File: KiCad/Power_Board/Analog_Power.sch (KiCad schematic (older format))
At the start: 73 parts, among them P10 CONN_02X01, P8 CONN_02X01, P9 CONN_02X01, Q1 IRLL024NQ, U10 ADP7142_CSP, U11 ADP7182_CSP, U12 ADP3335_CSP, U7 MAX152x, U8 ADP5070, U9 TPS63030

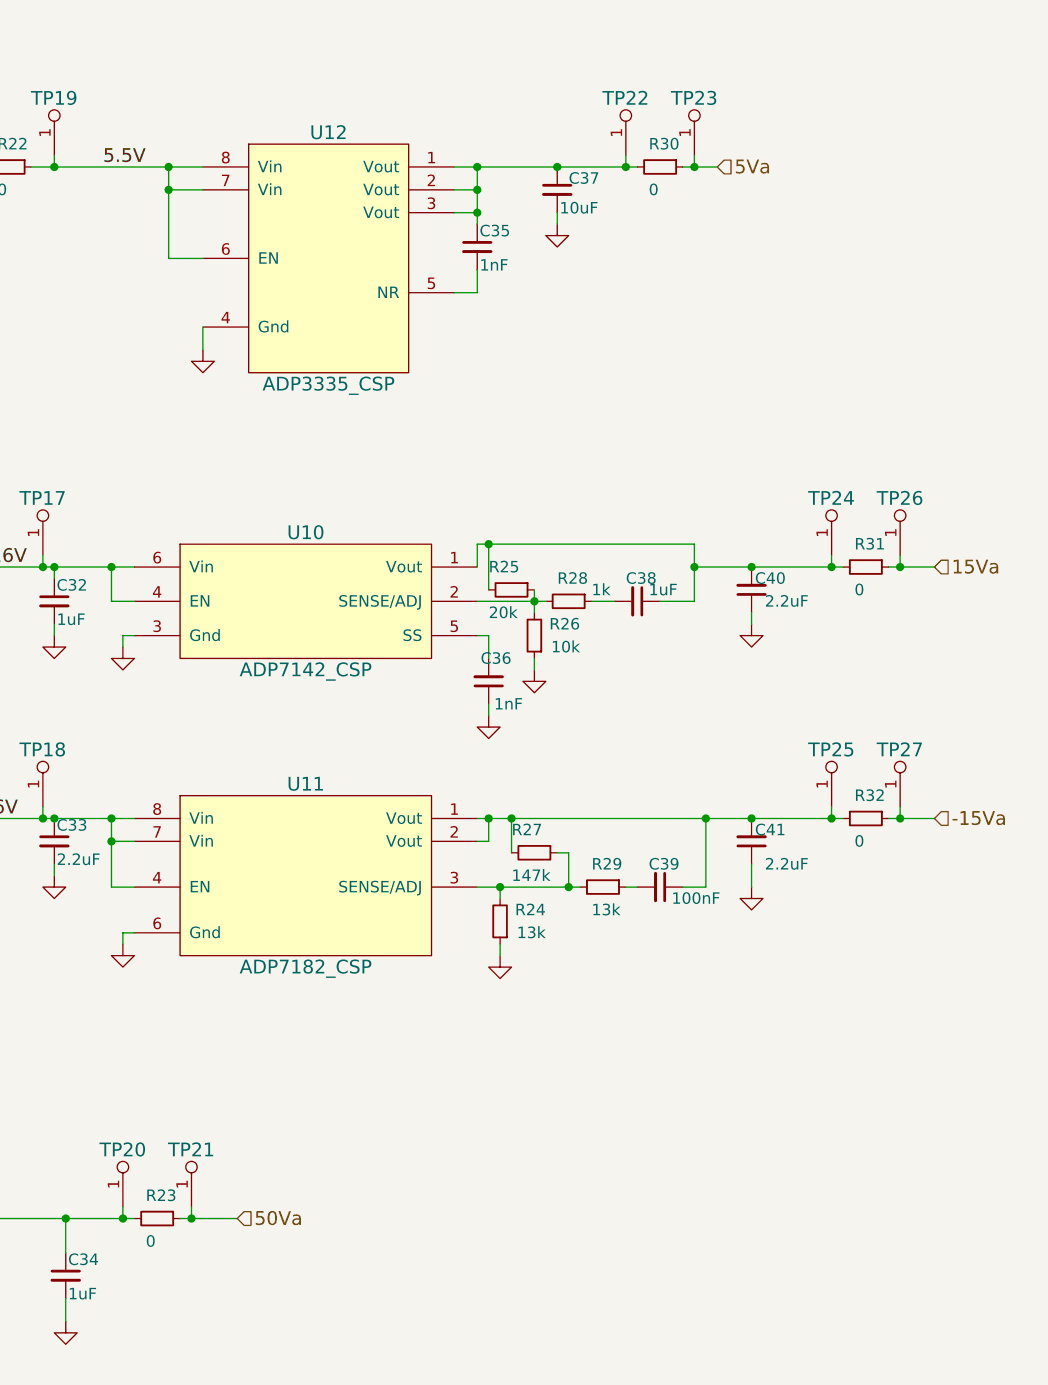
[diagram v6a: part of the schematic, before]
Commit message: Removed redundant SMD test points where test clips are being used.
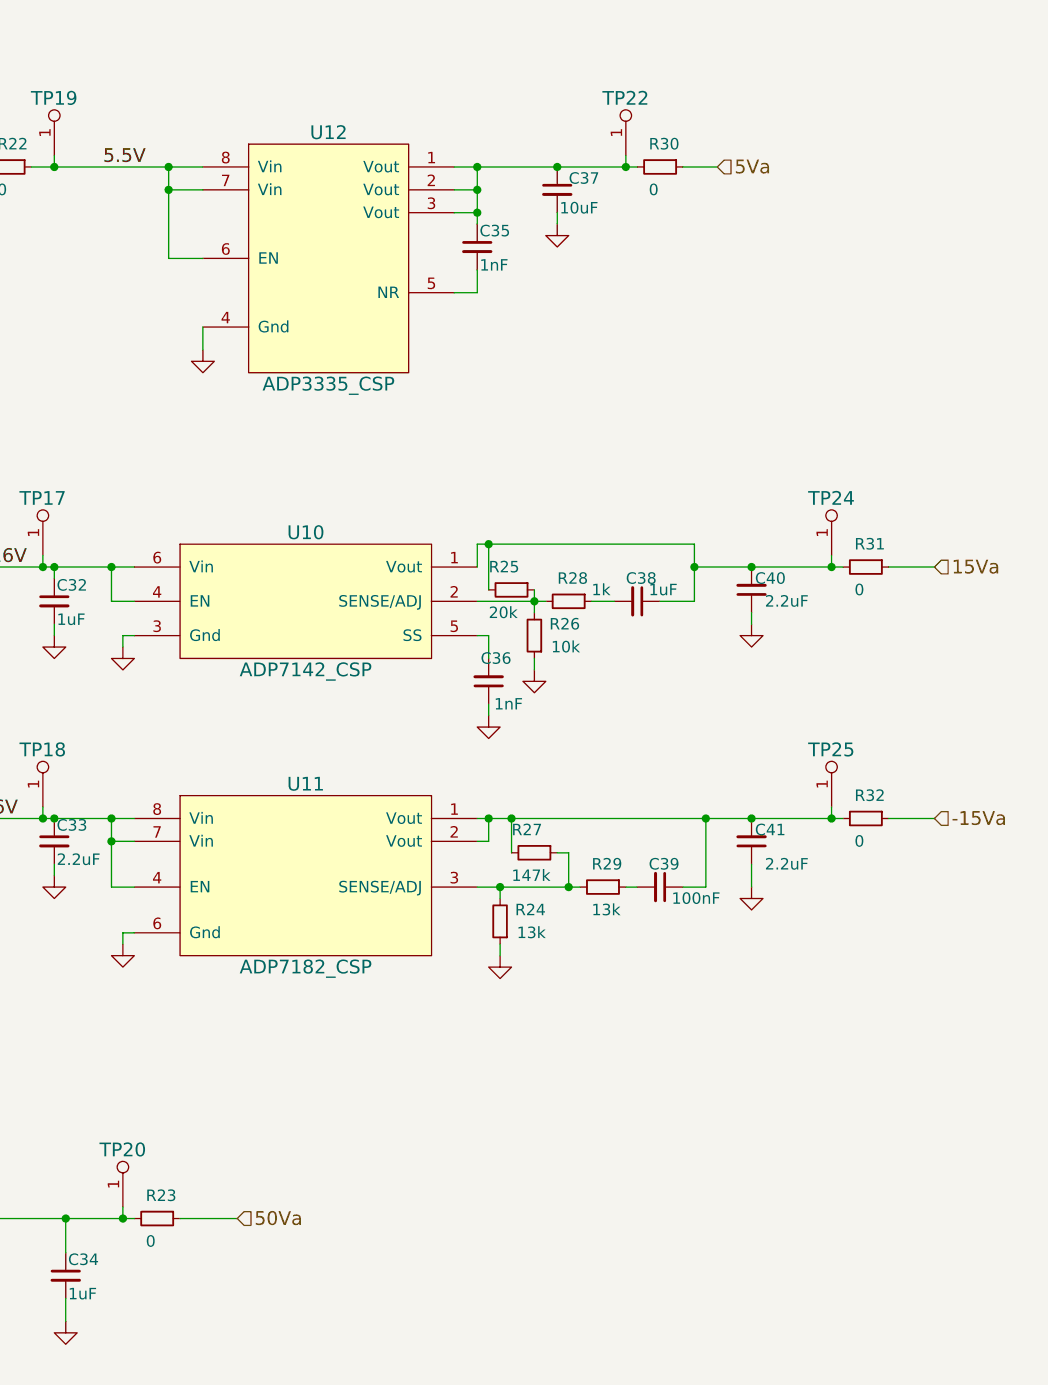
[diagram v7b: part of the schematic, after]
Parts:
- removed TP21, TP23, TP26, TP27: Test_Point, OpenCamera:TEST_POINT_SMD, symbol Test_Point
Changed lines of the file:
@@
 Connection ~ 5900 1400
 $Comp
-L GND #PWR033
+L GND #PWR035
 U 1 1 55902E67
 P 6050 2100
-F 0 "#PWR033" H 6050 1850 50  0001 C CNN
+F 0 "#PWR035" H 6050 1850 50  0001 C CNN
 F 1 "GND" H 6050 1950 50  0001 C CNN
 F 2 "" H 6050 2100 60  0000 C CNN
@@
 Wire Wire Line
 	8150 1300 8300 1300
-$Comp
-L Test_Point TP23
-U 1 1 559056BA
-P 8200 1250
-F 0 "TP23" H 8200 1500 60  0000 C CNN
-F 1 "Test_Point" H 8200 1600 60  0001 C CNN
-F 2 "OpenCamera:TEST_POINT_SMD" H 8200 1250 60  0001 C CNN
-F 3 "" H 8200 1250 60  0000 C CNN
-	1    8200 1250
-	1    0    0    -1
-$EndComp
 Wire Wire Line
 	7900 1250 7900 1300
 Connection ~ 7900 1300
-Wire Wire Line
-	8200 1250 8200 1300
-Connection ~ 8200 1300
-$Comp
-L GND #PWR034
+$Comp
+L GND #PWR036
 U 1 1 55900DFE
 P 4600 1850
-F 0 "#PWR034" H 4600 1600 50  0001 C CNN
+F 0 "#PWR036" H 4600 1600 50  0001 C CNN
 F 1 "GND" H 4600 1700 50  0001 C CNN
 F 2 "" H 4600 1850 60  0000 C CNN
@@
 $EndComp
 $Comp
-L GND #PWR035
+L GND #PWR037
 U 1 1 55900DF8
 P 4000 1850
-F 0 "#PWR035" H 4000 1600 50  0001 C CNN
+F 0 "#PWR037" H 4000 1600 50  0001 C CNN
 F 1 "GND" H 4000 1700 50  0001 C CNN
 F 2 "" H 4000 1850 60  0000 C CNN
@@
 $EndComp
 $Comp
-L GND #PWR036
+L GND #PWR038
 U 1 1 55900DF2
 P 3800 1850
-F 0 "#PWR036" H 3800 1600 50  0001 C CNN
+F 0 "#PWR038" H 3800 1600 50  0001 C CNN
 F 1 "GND" H 3800 1700 50  0001 C CNN
 F 2 "" H 3800 1850 60  0000 C CNN
@@
 $EndComp
 $Comp
-L GND #PWR037
+L GND #PWR039
 U 1 1 55900DDA
 P 2250 1800
-F 0 "#PWR037" H 2250 1550 50  0001 C CNN
+F 0 "#PWR039" H 2250 1550 50  0001 C CNN
 F 1 "GND" H 2250 1650 50  0001 C CNN
 F 2 "" H 2250 1800 60  0000 C CNN
@@
 	1600 2900 1500 2900
 $Comp
-L GND #PWR038
+L GND #PWR040
 U 1 1 5590B69B
 P 1250 2950
-F 0 "#PWR038" H 1250 2700 50  0001 C CNN
+F 0 "#PWR040" H 1250 2700 50  0001 C CNN
 F 1 "GND" H 1250 2800 50  0001 C CNN
 F 2 "" H 1250 2950 60  0000 C CNN
@@
 Connection ~ 1600 3450
 $Comp
-L GND #PWR039
+L GND #PWR041
 U 1 1 5590CBE4
 P 1550 4450
-F 0 "#PWR039" H 1550 4200 50  0001 C CNN
+F 0 "#PWR041" H 1550 4200 50  0001 C CNN
 F 1 "GND" H 1550 4300 50  0001 C CNN
 F 2 "" H 1550 4450 60  0000 C CNN
@@
 $EndComp
 $Comp
-L GND #PWR040
+L GND #PWR042
 U 1 1 5590CC43
 P 1600 3700
-F 0 "#PWR040" H 1600 3450 50  0001 C CNN
+F 0 "#PWR042" H 1600 3450 50  0001 C CNN
 F 1 "GND" H 1600 3550 50  0001 C CNN
 F 2 "" H 1600 3700 60  0000 C CNN
@@
 	1600 3950 1500 3950
 $Comp
-L GND #PWR041
+L GND #PWR043
 U 1 1 5590DECC
 P 1250 4100
-F 0 "#PWR041" H 1250 3850 50  0001 C CNN
+F 0 "#PWR043" H 1250 3850 50  0001 C CNN
 F 1 "GND" H 1250 3950 50  0001 C CNN
 F 2 "" H 1250 4100 60  0000 C CNN
@@
 	1250 3950 1250 4100
 $Comp
-L GND #PWR042
+L GND #PWR044
 U 1 1 5590E48E
 P 2700 4850
-F 0 "#PWR042" H 2700 4600 50  0001 C CNN
+F 0 "#PWR044" H 2700 4600 50  0001 C CNN
 F 1 "GND" H 2700 4700 50  0001 C CNN
 F 2 "" H 2700 4850 60  0000 C CNN
@@
 	1950 4300 1900 4300
 $Comp
-L GND #PWR043
+L GND #PWR045
 U 1 1 5590FDDF
 P 1900 4100
-F 0 "#PWR043" H 1900 3850 50  0001 C CNN
+F 0 "#PWR045" H 1900 3850 50  0001 C CNN
 F 1 "GND" H 1900 3950 50  0001 C CNN
 F 2 "" H 1900 4100 60  0000 C CNN
@@
 Connection ~ 4100 3050
 $Comp
-L GND #PWR044
+L GND #PWR046
 U 1 1 5591A3FF
 P 3600 3500
-F 0 "#PWR044" H 3600 3250 50  0001 C CNN
+F 0 "#PWR046" H 3600 3250 50  0001 C CNN
 F 1 "GND" H 3600 3350 50  0001 C CNN
 F 2 "" H 3600 3500 60  0000 C CNN
@@
 Connection ~ 3550 4150
 $Comp
-L GND #PWR045
+L GND #PWR047
 U 1 1 5591B69F
 P 3550 4850
-F 0 "#PWR045" H 3550 4600 50  0001 C CNN
+F 0 "#PWR047" H 3550 4600 50  0001 C CNN
 F 1 "GND" H 3550 4700 50  0001 C CNN
 F 2 "" H 3550 4850 60  0000 C CNN
@@
 Connection ~ 5650 4150
 $Comp
-L GND #PWR046
+L GND #PWR048
 U 1 1 5591C0E0
 P 5400 4400
-F 0 "#PWR046" H 5400 4150 50  0001 C CNN
+F 0 "#PWR048" H 5400 4150 50  0001 C CNN
 F 1 "GND" H 5400 4250 50  0001 C CNN
 F 2 "" H 5400 4400 60  0000 C CNN
@@
 Connection ~ 4200 4150
 $Comp
-L GND #PWR047
+L GND #PWR049
 U 1 1 5591CDF3
 P 4200 3750
-F 0 "#PWR047" H 4200 3500 50  0001 C CNN
+F 0 "#PWR049" H 4200 3500 50  0001 C CNN
 F 1 "GND" H 4200 3600 50  0001 C CNN
 F 2 "" H 4200 3750 60  0000 C CNN
@@
 Connection ~ 5400 3050
 $Comp
-L GND #PWR048
+L GND #PWR050
 U 1 1 5591DC9E
 P 5400 3350
-F 0 "#PWR048" H 5400 3100 50  0001 C CNN
+F 0 "#PWR050" H 5400 3100 50  0001 C CNN
 F 1 "GND" H 5400 3200 50  0001 C CNN
 F 2 "" H 5400 3350 60  0000 C CNN
@@
 	5400 3300 5400 3350
 $Comp
-L GND #PWR049
+L GND #PWR051
 U 1 1 5591DEAB
 P 5700 4700
-F 0 "#PWR049" H 5700 4450 50  0001 C CNN
+F 0 "#PWR051" H 5700 4450 50  0001 C CNN
 F 1 "GND" H 5700 4550 50  0001 C CNN
 F 2 "" H 5700 4700 60  0000 C CNN
@@
 $EndComp
 $Comp
-L GND #PWR050
+L GND #PWR052
 U 1 1 5591E006
 P 5700 3400
-F 0 "#PWR050" H 5700 3150 50  0001 C CNN
+F 0 "#PWR052" H 5700 3150 50  0001 C CNN
 F 1 "GND" H 5700 3250 50  0001 C CNN
 F 2 "" H 5700 3400 60  0000 C CNN
@@
 -15Va
 $Comp
-L GND #PWR051
+L GND #PWR053
 U 1 1 559206DA
 P 7300 3700
-F 0 "#PWR051" H 7300 3450 50  0001 C CNN
+F 0 "#PWR053" H 7300 3450 50  0001 C CNN
 F 1 "GND" H 7300 3550 50  0001 C CNN
 F 2 "" H 7300 3700 60  0000 C CNN
@@
 $EndComp
 $Comp
-L GND #PWR052
+L GND #PWR054
 U 1 1 55920835
 P 7500 3500
-F 0 "#PWR052" H 7500 3250 50  0001 C CNN
+F 0 "#PWR054" H 7500 3250 50  0001 C CNN
 F 1 "GND" H 7500 3350 50  0001 C CNN
 F 2 "" H 7500 3500 60  0000 C CNN
@@
 Connection ~ 8450 3050
 $Comp
-L GND #PWR053
+L GND #PWR055
 U 1 1 55921616
 P 8450 3300
-F 0 "#PWR053" H 8450 3050 50  0001 C CNN
+F 0 "#PWR055" H 8450 3050 50  0001 C CNN
 F 1 "GND" H 8450 3150 50  0001 C CNN
 F 2 "" H 8450 3300 60  0000 C CNN
@@
 $EndComp
 $Comp
-L GND #PWR054
+L GND #PWR056
 U 1 1 55922C11
 P 7350 4750
-F 0 "#PWR054" H 7350 4500 50  0001 C CNN
+F 0 "#PWR056" H 7350 4500 50  0001 C CNN
 F 1 "GND" H 7350 4600 50  0001 C CNN
 F 2 "" H 7350 4750 60  0000 C CNN
@@
 Connection ~ 8450 4150
 $Comp
-L GND #PWR055
+L GND #PWR057
 U 1 1 55924B3B
 P 8450 4450
-F 0 "#PWR055" H 8450 4200 50  0001 C CNN
+F 0 "#PWR057" H 8450 4200 50  0001 C CNN
 F 1 "GND" H 8450 4300 50  0001 C CNN
 F 2 "" H 8450 4450 60  0000 C CNN
@@
 Connection ~ 7650 4450
 $Comp
-L GND #PWR056
+L GND #PWR058
 U 1 1 5592A8F1
 P 7600 1550
-F 0 "#PWR056" H 7600 1300 50  0001 C CNN
+F 0 "#PWR058" H 7600 1300 50  0001 C CNN
 F 1 "GND" H 7600 1400 50  0001 C CNN
 F 2 "" H 7600 1550 60  0000 C CNN
@@
 Connection ~ 1700 6400
 $Comp
-L GND #PWR057
+L GND #PWR059
 U 1 1 5592C7CC
 P 1700 7000
-F 0 "#PWR057" H 1700 6750 50  0001 C CNN
+F 0 "#PWR059" H 1700 6750 50  0001 C CNN
 F 1 "GND" H 1700 6850 50  0001 C CNN
 F 2 "" H 1700 7000 60  0000 C CNN
@@
 50Va
 $Comp
-L GND #PWR058
+L GND #PWR060
 U 1 1 55930BA5
 P 3350 6450
-F 0 "#PWR058" H 3350 6200 50  0001 C CNN
+F 0 "#PWR060" H 3350 6200 50  0001 C CNN
 F 1 "GND" H 3350 6300 50  0001 C CNN
 F 2 "" H 3350 6450 60  0000 C CNN
@@
 	3350 6400 3350 6450
 $Comp
-L GND #PWR059
+L GND #PWR061
 U 1 1 55930F0C
 P 4400 7000
-F 0 "#PWR059" H 4400 6750 50  0001 C CNN
+F 0 "#PWR061" H 4400 6750 50  0001 C CNN
 F 1 "GND" H 4400 6850 50  0001 C CNN
 F 2 "" H 4400 7000 60  0000 C CNN
@@
 Connection ~ 4950 5900
 $Comp
-L GND #PWR060
+L GND #PWR062
 U 1 1 5593242A
 P 5450 6350
-F 0 "#PWR060" H 5450 6100 50  0001 C CNN
+F 0 "#PWR062" H 5450 6100 50  0001 C CNN
 F 1 "GND" H 5450 6200 50  0001 C CNN
 F 2 "" H 5450 6350 60  0000 C CNN
@@
 Gnd
 $Comp
-L GND #PWR061
+L GND #PWR063
 U 1 1 559360C9
 P 900 1750
-F 0 "#PWR061" H 900 1500 50  0001 C CNN
+F 0 "#PWR063" H 900 1500 50  0001 C CNN
 F 1 "GND" H 900 1600 50  0001 C CNN
 F 2 "" H 900 1750 60  0000 C CNN
@@
 Wire Wire Line
 	5950 5900 6200 5900
-$Comp
-L Test_Point TP21
-U 1 1 558FB360
-P 6000 5850
-F 0 "TP21" H 6000 6100 60  0000 C CNN
-F 1 "Test_Point" H 6000 6200 60  0001 C CNN
-F 2 "OpenCamera:TEST_POINT_SMD" H 6000 5850 60  0001 C CNN
-F 3 "" H 6000 5850 60  0000 C CNN
-	1    6000 5850
-	1    0    0    -1
-$EndComp
 Wire Wire Line
 	5700 5900 5700 5850
 Connection ~ 5700 5900
-Wire Wire Line
-	6000 5850 6000 5900
-Connection ~ 6000 5900
 $Comp
 L Test_Point TP25
@@
 Wire Wire Line
 	9050 4150 9250 4150
-$Comp
-L Test_Point TP27
-U 1 1 558FC570
-P 9100 4100
-F 0 "TP27" H 9100 4350 60  0000 C CNN
-F 1 "Test_Point" H 9100 4450 60  0001 C CNN
-F 2 "OpenCamera:TEST_POINT_SMD" H 9100 4100 60  0001 C CNN
-F 3 "" H 9100 4100 60  0000 C CNN
-	1    9100 4100
-	1    0    0    -1
-$EndComp
 Wire Wire Line
 	8800 4150 8800 4100
 Connection ~ 8800 4150
-Wire Wire Line
-	9100 4100 9100 4150
-Connection ~ 9100 4150
 $Comp
 L Test_Point TP24
@@
 Wire Wire Line
 	9050 3050 9250 3050
-$Comp
-L Test_Point TP26
-U 1 1 558FC9A5
-P 9100 3000
-F 0 "TP26" H 9100 3250 60  0000 C CNN
-F 1 "Test_Point" H 9100 3350 60  0001 C CNN
-F 2 "OpenCamera:TEST_POINT_SMD" H 9100 3000 60  0001 C CNN
-F 3 "" H 9100 3000 60  0000 C CNN
-	1    9100 3000
-	1    0    0    -1
-$EndComp
 Wire Wire Line
 	8800 3050 8800 3000
 Connection ~ 8800 3050
 Wire Wire Line
-	9100 3000 9100 3050
-Connection ~ 9100 3050
-Wire Wire Line
 	7400 4300 7400 4150

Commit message: Some layout progress.
Properly placed and oriented parts for compact layout of individual
modules.
Added zones of copper around the converters as appropriate.
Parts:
- D4: footprint Diodes_ThroughHole:Diode_DO-35_SOD27_Horizontal_RM10 -> OpenCamera:Diode_DO-35
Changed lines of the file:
@@
 F 0 "D4" V 4450 6350 50  0000 L CNN
 F 1 "1N5261" V 4350 6150 50  0000 L CNN
-F 2 "Diodes_ThroughHole:Diode_DO-35_SOD27_Horizontal_RM10" V 4400 6500 60  0001 C CNN
+F 2 "OpenCamera:Diode_DO-35" V 4400 6500 60  0001 C CNN
 F 3 "" V 4400 6500 60  0000 C CNN
 	1    4400 6500
